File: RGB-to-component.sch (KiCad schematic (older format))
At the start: 60 parts, among them J1 VGA, J3 USB_C_Receptacle_Power, J4 SCART_CONN, J5 3xRCA_CONN, U1 SC6206B-65K5, U101 TPF144-VR, U2 TPF144-VR, U3 RS8752XM, U6 74AHCT1G86, U7 74AHCT1G86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

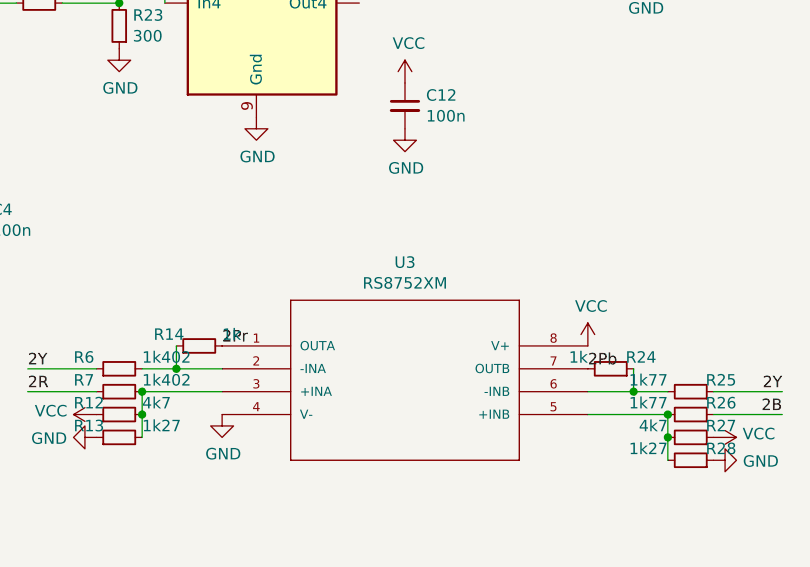
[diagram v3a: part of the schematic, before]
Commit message: swapped opamp for SOIC package
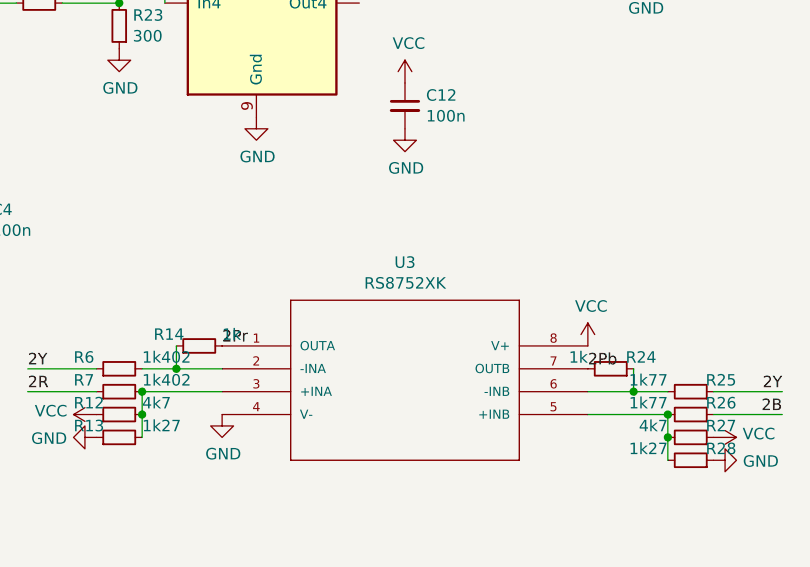
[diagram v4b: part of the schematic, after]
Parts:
- U3: value RS8752XM -> RS8752XK; footprint Package_SO:MSOP-8_3x3mm_P0.65mm -> Package_SO:SOIC-8_3.9x4.9mm_P1.27mm; LCSC C255421 -> C236994
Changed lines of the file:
@@
 P 7950 3600
 F 0 "U3" H 8750 3965 50  0000 C CNN
-F 1 "RS8752XM" H 8750 3874 50  0000 C CNN
-F 2 "Package_SO:MSOP-8_3x3mm_P0.65mm" H 7950 3600 50  0001 L BNN
+F 1 "RS8752XK" H 8750 3874 50  0000 C CNN
+F 2 "Package_SO:SOIC-8_3.9x4.9mm_P1.27mm" H 7950 3600 50  0001 L BNN
 F 3 "" H 7950 3600 50  0001 L BNN
 F 4 "" H 7950 3600 50  0001 L BNN "Field4"
@@
 F 7 "" H 7950 3600 50  0001 L BNN "Field7"
 F 8 "" H 7950 3600 50  0000 L BNN "Field8"
-F 9 "C255421" H 7950 3600 50  0001 C CNN "LCSC"
+F 9 "C236994" H 7950 3600 50  0001 C CNN "LCSC"
 	1    7950 3600
 	1    0    0    -1
